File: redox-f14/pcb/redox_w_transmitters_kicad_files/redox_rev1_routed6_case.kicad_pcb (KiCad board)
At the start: 2 copper layers, 145.8 x 126.5 mm, 31 parts, among them K0 KEYSW, K1 KEYSW, K10 KEYSW, K11 KEYSW, K12 KEYSW, K13 KEYSW, K14 KEYSW, K15 KEYSW, K16 KEYSW, K2 KEYSW, K20 KEYSW, K21 KEYSW, K22 KEYSW, K23 KEYSW, K24 KEYSW, K25 KEYSW, K26 KEYSW, K3 KEYSW, K30 KEYSW, K31 KEYSW, K32 KEYSW, K33 KEYSW, K34 KEYSW, K35 KEYSW, K4 KEYSW, K42 KEYSW, K43 KEYSW, K44 KEYSW, K45 KEYSW, K5 KEYSW, K6 KEYSW

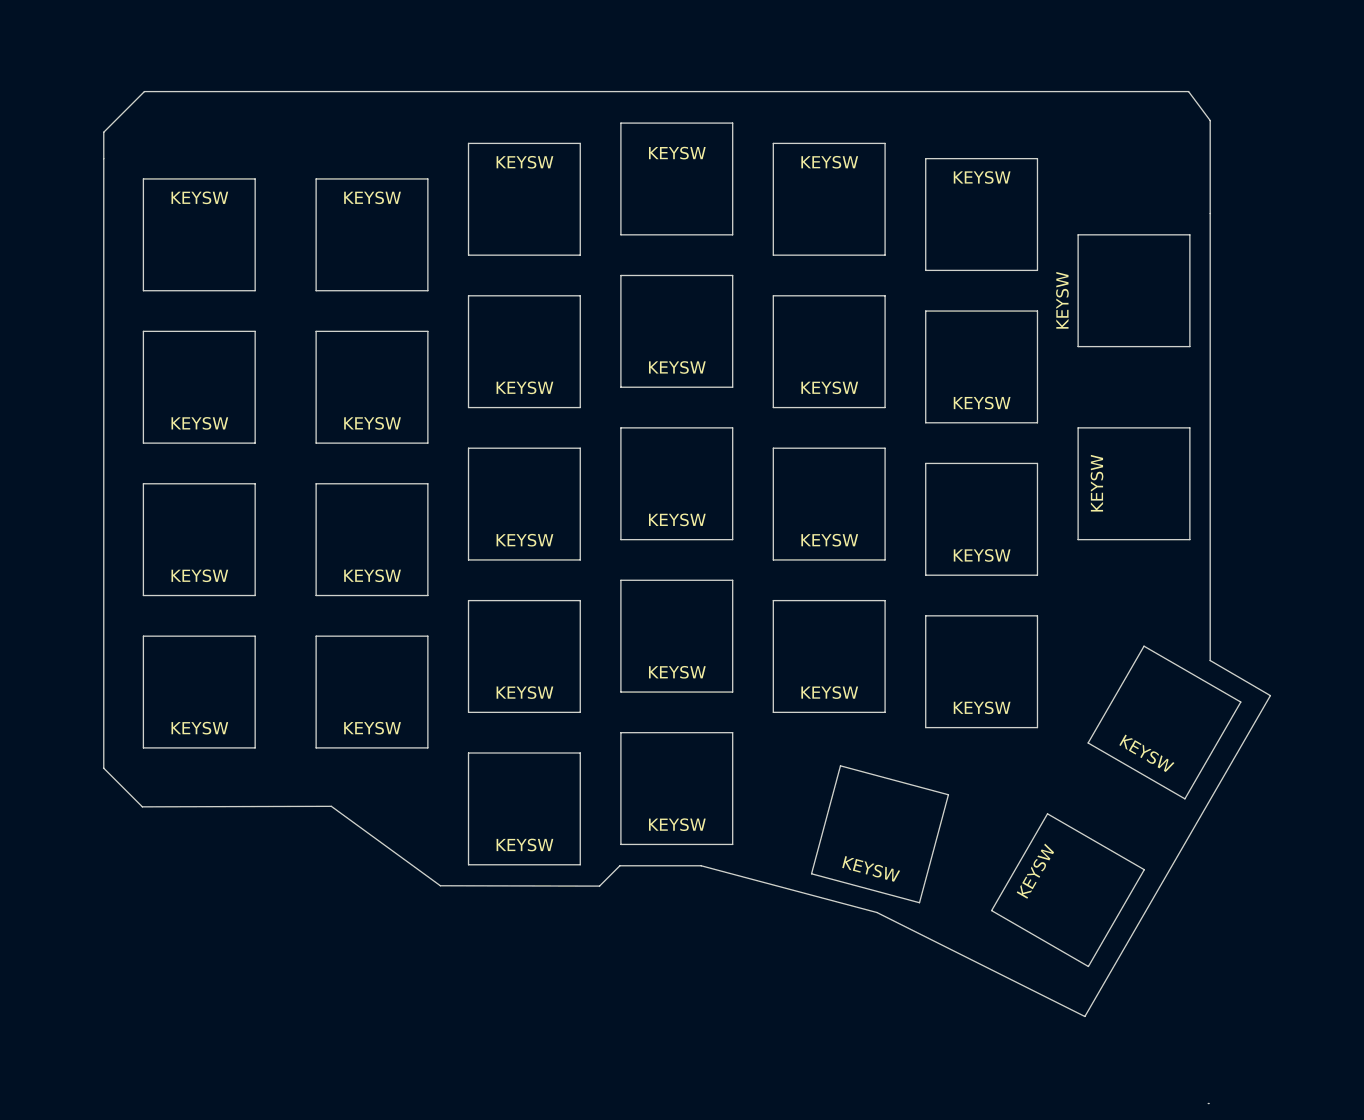
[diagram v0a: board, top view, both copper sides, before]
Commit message: add case files
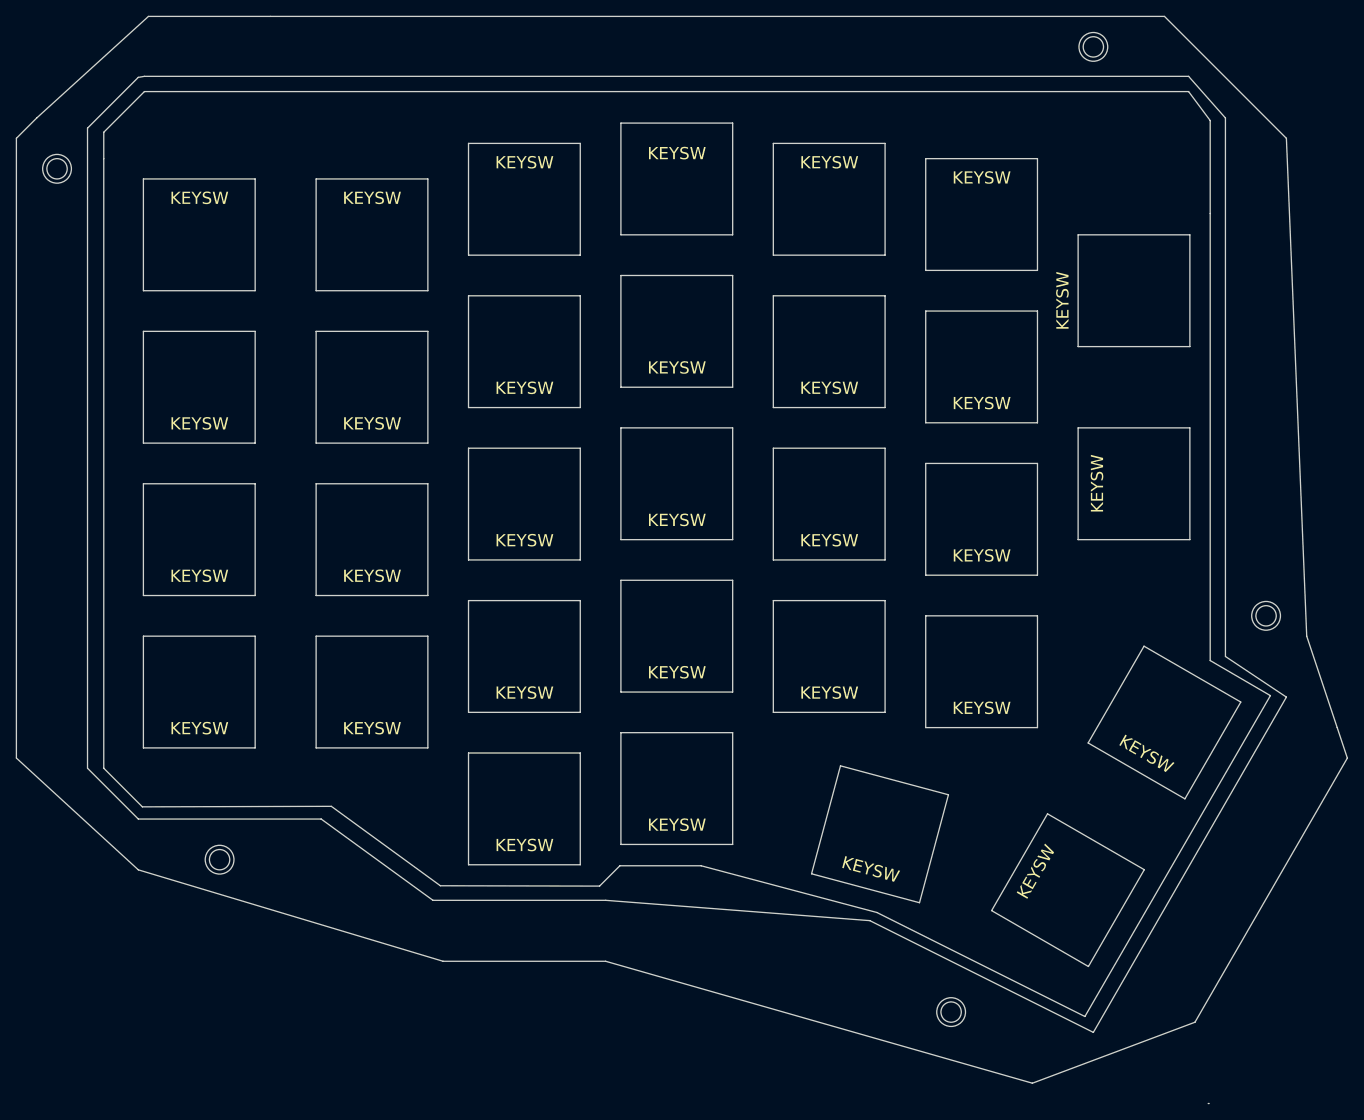
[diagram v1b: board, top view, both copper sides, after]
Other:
- board size 145.8 x 126.5 mm -> 166.4 x 135.9 mm
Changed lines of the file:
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@@
   (general
     (thickness 1.6)
-    (drawings 18)
+    (drawings 57)
     (tracks 0)
     (zones 0)
@@
     )
   )
+  (gr_circle (center 73.66 58.42) (end 74.93 58.42) (layer Edge.Cuts) (width 0.1))
+  (gr_circle (center 203.2 43.18) (end 204.47 43.18) (layer Edge.Cuts) (width 0.1))
+  (gr_circle (center 224.79 114.3) (end 226.06 114.3) (layer Edge.Cuts) (width 0.1))
+  (gr_circle (center 185.42 163.83) (end 186.69 163.83) (layer Edge.Cuts) (width 0.1))
+  (gr_circle (center 93.98 144.78) (end 95.25 144.78) (layer Edge.Cuts) (width 0.1))
+  (gr_circle (center 203.2 43.18) (end 204.47 44.45) (layer Edge.Cuts) (width 0.1))
+  (gr_circle (center 73.66 58.42) (end 74.93 59.69) (layer Edge.Cuts) (width 0.1))
+  (gr_circle (center 93.98 144.78) (end 95.25 146.05) (layer Edge.Cuts) (width 0.1))
+  (gr_circle (center 185.42 163.83) (end 186.69 165.1) (layer Edge.Cuts) (width 0.1))
+  (gr_circle (center 224.79 114.3) (end 226.06 115.57) (layer Edge.Cuts) (width 0.1))
+  (gr_line (start 83.82 46.99) (end 84.582 46.863) (layer Edge.Cuts) (width 0.1))
+  (gr_line (start 77.47 53.34) (end 83.82 46.99) (layer Edge.Cuts) (width 0.1))
+  (gr_line (start 79.502 53.848) (end 79.502 57.15) (angle 90) (layer Edge.Cuts) (width 0.1))
+  (gr_line (start 79.502 53.848) (end 84.582 48.768) (angle 90) (layer Edge.Cuts) (width 0.1))
+  (gr_line (start 77.47 133.35) (end 77.47 53.34) (layer Edge.Cuts) (width 0.1))
+  (gr_line (start 83.82 139.7) (end 77.47 133.35) (layer Edge.Cuts) (width 0.1))
+  (gr_line (start 106.68 139.7) (end 83.82 139.7) (layer Edge.Cuts) (width 0.1))
+  (gr_line (start 120.65 149.86) (end 106.68 139.7) (layer Edge.Cuts) (width 0.1))
+  (gr_line (start 142.24 149.86) (end 120.65 149.86) (layer Edge.Cuts) (width 0.1))
+  (gr_line (start 175.26 152.4) (end 142.24 149.86) (layer Edge.Cuts) (width 0.1))
+  (gr_line (start 203.2 166.37) (end 175.26 152.4) (layer Edge.Cuts) (width 0.1))
+  (gr_line (start 227.33 124.46) (end 203.2 166.37) (layer Edge.Cuts) (width 0.1))
+  (gr_line (start 219.71 119.38) (end 227.33 124.46) (layer Edge.Cuts) (width 0.1))
+  (gr_line (start 219.71 52.07) (end 219.71 119.38) (layer Edge.Cuts) (width 0.1))
+  (gr_line (start 215.10625 46.863) (end 219.71 52.07) (layer Edge.Cuts) (width 0.1))
+  (gr_line (start 215.10625 46.863) (end 84.582 46.863) (angle 90) (layer Edge.Cuts) (width 0.1))
+  (gr_line (start 68.58 54.61) (end 68.58 132.08) (layer Edge.Cuts) (width 0.1))
+  (gr_line (start 71.12 52.07) (end 68.58 54.61) (layer Edge.Cuts) (width 0.1))
+  (gr_line (start 71.12 52.07) (end 85.09 39.37) (layer Edge.Cuts) (width 0.1))
+  (gr_line (start 83.82 146.05) (end 68.58 132.08) (layer Edge.Cuts) (width 0.1))
+  (gr_line (start 121.92 157.48) (end 83.82 146.05) (layer Edge.Cuts) (width 0.1))
+  (gr_line (start 142.24 157.48) (end 121.92 157.48) (layer Edge.Cuts) (width 0.1))
+  (gr_line (start 195.58 172.72) (end 142.24 157.48) (layer Edge.Cuts) (width 0.1))
+  (gr_line (start 215.9 165.1) (end 195.58 172.72) (layer Edge.Cuts) (width 0.1))
+  (gr_line (start 234.95 132.08) (end 215.9 165.1) (layer Edge.Cuts) (width 0.1))
+  (gr_line (start 233.68 128.27) (end 234.95 132.08) (layer Edge.Cuts) (width 0.1))
+  (gr_line (start 229.87 116.84) (end 233.68 128.27) (layer Edge.Cuts) (width 0.1))
+  (gr_line (start 227.33 54.61) (end 229.87 116.84) (layer Edge.Cuts) (width 0.1))
+  (gr_line (start 212.09 39.37) (end 227.33 54.61) (layer Edge.Cuts) (width 0.1))
+  (gr_line (start 100.33 39.37) (end 212.09 39.37) (layer Edge.Cuts) (width 0.1))
+  (gr_line (start 85.09 39.37) (end 100.33 39.37) (layer Edge.Cuts) (width 0.1))
   (gr_line (start 215.10625 48.768) (end 217.805 52.3875) (layer Edge.Cuts) (width 0.1))
   (gr_line (start 107.95 138.1125) (end 84.328 138.176) (layer Edge.Cuts) (width 0.1))
@@
   (gr_line (start 215.10625 48.768) (end 84.582 48.768) (angle 90) (layer Edge.Cuts) (width 0.1))
   (gr_line (start 217.805 52.3875) (end 217.805 64.008) (angle 90) (layer Edge.Cuts) (width 0.1))
-  (gr_line (start 79.502 53.848) (end 79.502 57.15) (angle 90) (layer Edge.Cuts) (width 0.1))
-  (gr_line (start 79.502 53.848) (end 84.582 48.768) (angle 90) (layer Edge.Cuts) (width 0.1))
   (gr_line (start 154.178 145.542) (end 144.018 145.542) (angle 90) (layer Edge.Cuts) (width 0.1))
   (gr_line (start 217.805 119.888) (end 225.330156 124.273242) (angle 90) (layer Edge.Cuts) (width 0.1))

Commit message: update case v2
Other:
- board size 166.4 x 135.9 mm -> 164.3 x 134.8 mm
